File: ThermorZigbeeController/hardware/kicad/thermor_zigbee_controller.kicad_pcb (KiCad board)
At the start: 2 copper layers, 80 x 60 mm, 7 parts, among them J1 PIR_Sensor, U1 ESP32-C6-WROOM-1, U2 HT1621, U3 PC817

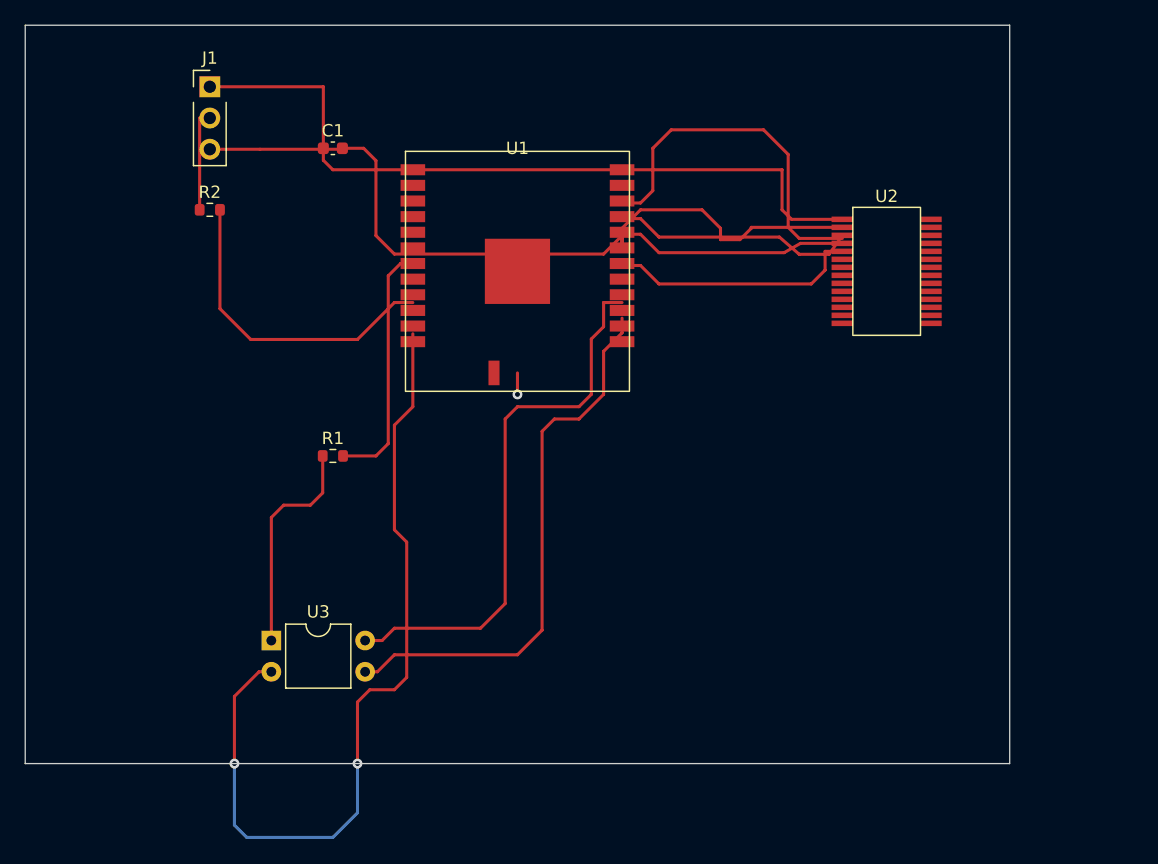
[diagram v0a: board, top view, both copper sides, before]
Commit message: fix: Replace PCB file with valid KiCad 7.0 format
- Create new PCB file with correct syntax and structure
- Fix all parentheses and formatting issues
- Add complete component placement for:
  - ESP32-C6-WROOM-1 (QFN-40 package)
  - HT1621 LCD controller (SSOP-20)
  - PC817 optocoupler (DIP-4)
  - PIR sensor connector (JST-XH 3P)
  - Pull-up resistor and decoupling capacitor
- Add basic routing for critical signals
- Include ground plane on bottom layer
- Set board dimensions to 80x60mm

The PCB file now opens correctly in KiCad 7.0.

🤖 Generated with Claude Code

Co-Authored-By: Claude <noreply@anthropic.com>
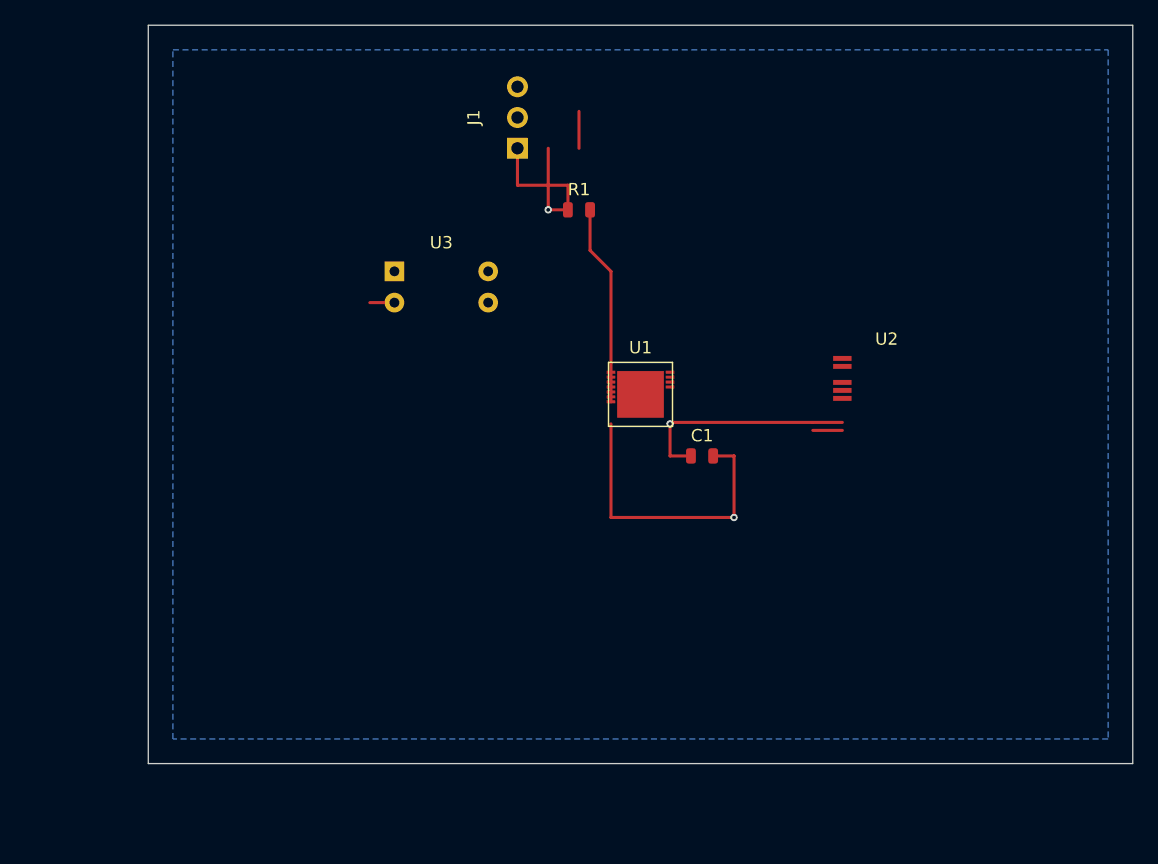
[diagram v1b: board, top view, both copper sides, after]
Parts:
- removed R2: 10k, Resistor_SMD:R_0603_1608Metric
- C1: footprint Capacitor_SMD:C_0603_1608Metric -> Capacitor_SMD:C_0805_2012Metric
- J1: value PIR_Sensor -> PIR_SENSOR; footprint Connector_PinHeader_2.54mm:PinHeader_1x03_P2.54mm_Vertical -> Connector_JST:JST_XH_B3B-XH-A_1x03_P2.50mm_Vertical
- R1: value 1k -> 10k; footprint Resistor_SMD:R_0603_1608Metric -> Resistor_SMD:R_0805_2012Metric
- U1: footprint RF_Module:ESP32-C6-WROOM-1 -> Package_DFN_QFN:QFN-40-1EP_5x5mm_P0.4mm_EP3.8x3.8mm
- U2: footprint Package_SO:SSOP-28_5.3x10.2mm_P0.65mm -> Package_SO:SSOP-20_5.3x7.2mm_P0.65mm
- moved C1 39.1 mm to (155.0, 135.0)
- moved U3 31.6 mm to (130.0, 120.0)
- moved R1 28.3 mm to (145.0, 115.0)
- moved J1 25.5 mm to (140.0, 110.0), turned to 90 degrees
- moved U1 14.1 mm to (150.0, 130.0)
- moved U2 10.0 mm to (170.0, 130.0)
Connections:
- net Net-(U1-IO23) renamed /TEMP_SENS
- net Net-(U1-IO6) renamed /TRIAC2
- J1 pad 2: Net-(U4-OUT) -> /PIR_OUT
- R1 pad 1: Net-(U3-A) -> +3V3
- R1 pad 2: Net-(U1-IO8) -> /PIR_OUT
- U1 pad 1: +3V3 -> GND
- U1 pad 15: Net-(U1-IO20) -> /LCD_CS
- U1 pad 16: Net-(U1-IO21) -> /LCD_WR
- U1 pad 17: Net-(U1-IO22) -> /LCD_DATA
- U1 pad 2: Net-(U1-EN) -> +3V3
- U1 pad 3: Net-(U1-IO4) -> +3V3
- U1 pad 4: Net-(U1-IO5) -> /TRIAC1
- U1 pad 6: Net-(U1-IO7) -> /ZERO_CROSS
- U1 pad 7: Net-(U1-IO8) -> /PIR_OUT
- U2 pad 1: +3V3 -> GND
- U2 pad 2: GND -> +3V3
- U2 pad 4: Net-(U2-WR) -> /LCD_CS
- U2 pad 5: Net-(U2-DATA) -> /LCD_WR
- U2 pad 6: (no net) -> /LCD_DATA
- U3 pad 1: Net-(U3-A) -> /TRIAC1
- U3 pad 2: Net-(U3-K) -> GND
- U3 pad 3: Net-(U3-E) -> (no net)
- U3 pad 4: Net-(U3-C) -> /ZERO_CROSS
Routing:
- net Net-(U3-K): track 68.3 -> 0.00 mm, vias 2 -> 0
- net Net-(U3-E): track 45.0 -> 0.00 mm
- net Net-(U3-C): track 44.8 -> 0.00 mm
- net GND: track 66.2 -> 31.7 mm
- net +3V3: track 61.3 -> 27.4 mm, vias 0 -> 1
- net Net-(U1-IO4): track 29.5 -> 0.00 mm
- net Net-(U1-IO10): track 26.0 -> 0.00 mm
- net /PIR_OUT: track 0.00 -> 22.9 mm, vias 0 -> 1
- net Net-(U2-DATA): track 20.5 -> 0.00 mm
- net Net-(U1-IO8): track 20.1 -> 0.00 mm
- net Net-(U2-CS): track 19.8 -> 0.00 mm
- net Net-(U2-WR): track 18.7 -> 0.00 mm
- net Net-(U3-A): track 18.0 -> 0.00 mm
- net Net-(U4-OUT): track 8.28 -> 0.00 mm
- added copper zone on B.Cu, net GND
